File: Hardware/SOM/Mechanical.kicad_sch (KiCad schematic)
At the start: 1 part, among them J1 SODIMM-200_Split

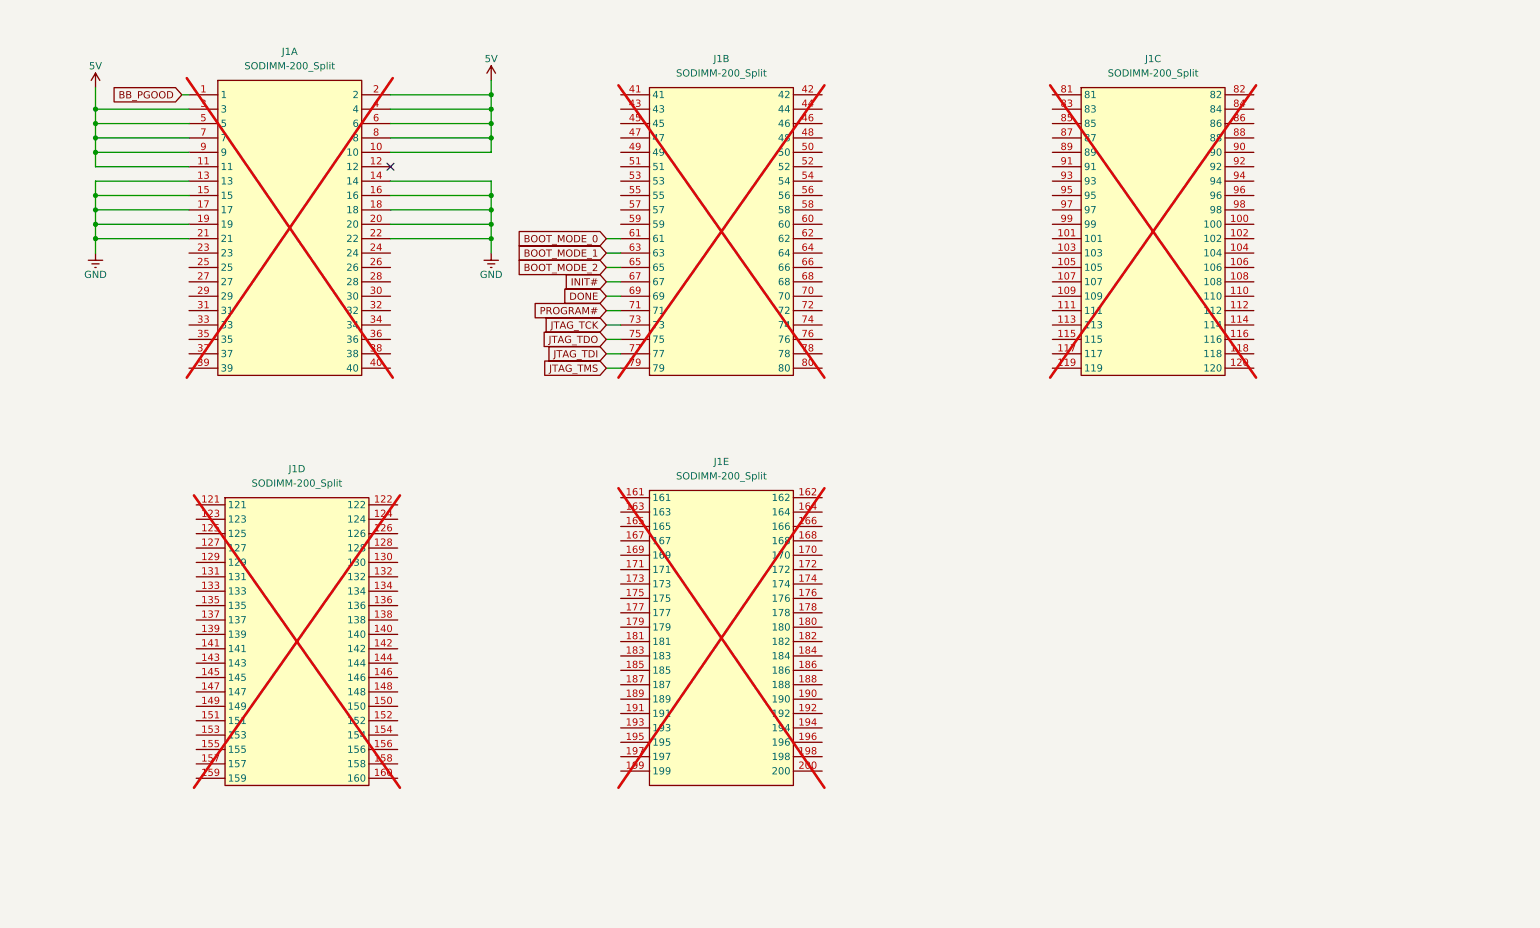
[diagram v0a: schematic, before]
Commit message: SOM: decoupling caps placement
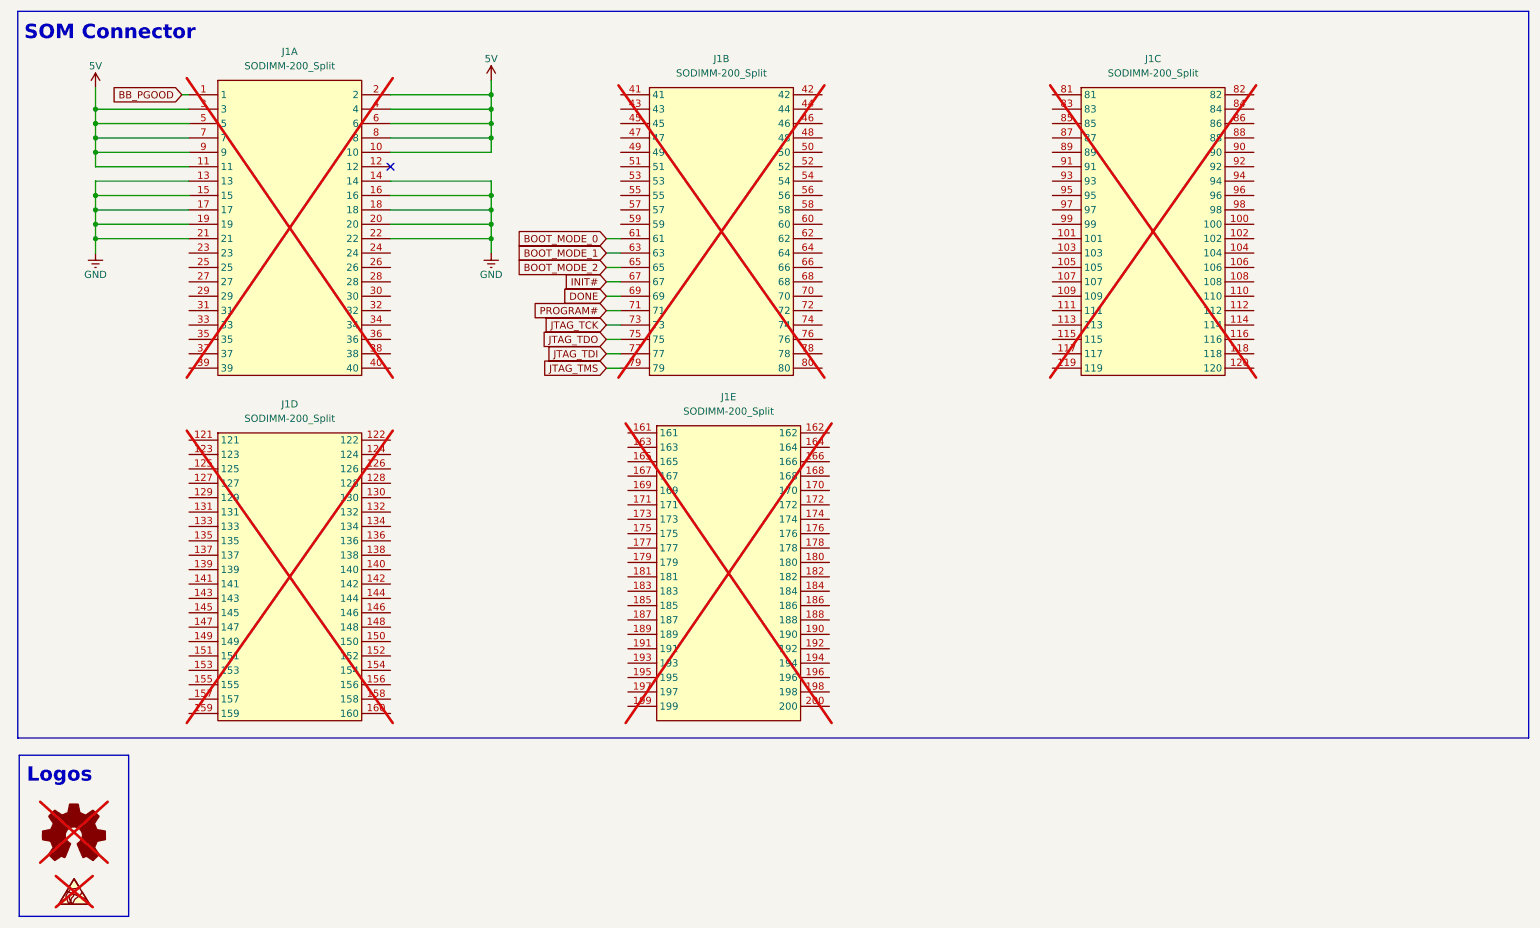
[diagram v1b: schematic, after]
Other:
- note added: "Logos"
- note added: "SOM Connector"
- moved on the sheet: J1D, J1E
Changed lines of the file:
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@@
 	(generator_version "9.0")
 	(paper "A4")
+	(rectangle
+		(start 15.494 15.748)
+		(end 282.194 144.018)
+		(stroke
+			(width 0)
+			(type default)
+		)
+		(fill
+			(type none)
+		)
+	)
+	(rectangle
+		(start 15.748 147.066)
+		(end 35.052 175.514)
+		(stroke
+			(width 0)
+			(type default)
+		)
+		(fill
+			(type none)
+		)
+	)
+	(text "Logos"
+		(exclude_from_sim no)
+		(at 22.86 150.622 0)
+		(effects
+			(font
+				(size 2.54 2.54)
+				(thickness 0.254)
+				(bold yes)
+			)
+		)
+	)
+	(text "SOM Connector"
+		(exclude_from_sim no)
+		(at 31.75 19.558 0)
+		(effects
+			(font
+				(size 2.54 2.54)
+				(thickness 0.254)
+				(bold yes)
+			)
+		)
+	)
 	(junction
 		(at 99.06 35.56)
@@
 	)
 	(symbol
+		(lib_id "Graphic:SYM_ESD_Small")
+		(at 25.4 171.45 0)
+		(unit 1)
+		(exclude_from_sim no)
+		(in_bom yes)
+		(on_board yes)
+		(dnp yes)
+		(fields_autoplaced yes)
+		(property "Reference" "#SYM2"
+			(at 25.4 167.894 0)
+			(effects
+				(font
+					(size 1.27 1.27)
+				)
+				(hide yes)
+			)
+		)
+		(property "Value" "SYM_ESD_Small"
+			(at 25.4 174.625 0)
+			(effects
+				(font
+					(size 1.27 1.27)
+				)
+				(hide yes)
+			)
+		)
+		(property "Footprint" "Symbol:ESD-Logo_6.6x6mm_SilkScreen"
+			(at 25.4 171.196 0)
+			(effects
+				(font
+					(size 1.27 1.27)
+				)
+				(hide yes)
+			)
+		)
+		(property "Datasheet" "~"
+			(at 25.4 171.196 0)
+			(effects
+				(font
+					(size 1.27 1.27)
+				)
+				(hide yes)
+			)
+		)
+		(property "Description" "ESD warning/\"Do not touch\" symbol, small"
+			(at 25.4 171.45 0)
+			(effects
+				(font
+					(size 1.27 1.27)
+				)
+				(hide yes)
+			)
+		)
+		(instances
+			(project ""
+				(path "/de32abb0-ff3b-4c67-a91a-eed08140b1b2/5afb2ac4-dadb-4f86-a03f-bc72f6fc34d4"
+					(reference "#SYM2")
+					(unit 1)
+				)
+			)
+		)
+	)
+	(symbol
 		(lib_id "power:+1V5")
 		(at 99.06 27.94 0)
@@
 	(symbol
 		(lib_id "Connector:SODIMM-200_Split")
-		(at 64.77 125.73 0)
+		(at 63.5 114.3 0)
 		(unit 4)
 		(exclude_from_sim no)
@@
 		(fields_autoplaced yes)
 		(property "Reference" "J1"
-			(at 64.77 96.52 0)
+			(at 63.5 85.09 0)
 			(effects
 				(font
@@
 		)
 		(property "Value" "SODIMM-200_Split"
-			(at 64.77 99.06 0)
+			(at 63.5 87.63 0)
 			(effects
 				(font
@@
 		)
 		(property "Footprint" "Connector_PCBEdge:SODIMM-200_1.8V_Card_edge"
-			(at 100.33 104.14 0)
+			(at 99.06 92.71 0)
 			(effects
 				(font
@@
 		)
 		(property "Datasheet" "~"
-			(at 100.33 104.14 0)
+			(at 99.06 92.71 0)
 			(effects
 				(font
@@
 		)
 		(property "Description" "SODIMM 200 Pin socket"
-			(at 64.77 125.73 0)
+			(at 63.5 114.3 0)
 			(effects
 				(font
@@
 		)
 		(property "Manufacturer" "TE Connectivity "
-			(at 64.77 125.73 0)
+			(at 63.5 114.3 0)
 			(effects
 				(font
@@
 		)
 		(property "MPN" "1473005-4 "
-			(at 64.77 125.73 0)
+			(at 63.5 114.3 0)
 			(effects
 				(font
@@
 					(reference "J1")
 					(unit 4)
+				)
+			)
+		)
+	)
+	(symbol
+		(lib_id "Graphic:Logo_Open_Hardware_Small")
+		(at 25.4 161.29 0)
+		(unit 1)
+		(exclude_from_sim no)
+		(in_bom yes)
+		(on_board yes)
+		(dnp yes)
+		(fields_autoplaced yes)
+		(property "Reference" "#SYM1"
+			(at 25.4 154.305 0)
+			(effects
+				(font
+					(size 1.27 1.27)
+				)
+				(hide yes)
+			)
+		)
+		(property "Value" "Logo_Open_Hardware_Small"
+			(at 25.4 167.005 0)
+			(effects
+				(font
+					(size 1.27 1.27)
+				)
+				(hide yes)
+			)
+		)
+		(property "Footprint" "Symbol:OSHW-Logo_5.7x6mm_Copper"
+			(at 25.4 161.29 0)
+			(effects
+				(font
+					(size 1.27 1.27)
+				)
+				(hide yes)
+			)
+		)
+		(property "Datasheet" "~"
+			(at 25.4 161.29 0)
+			(effects
+				(font
+					(size 1.27 1.27)
+				)
+				(hide yes)
+			)
+		)
+		(property "Description" "Open Hardware logo, small"
+			(at 25.4 161.29 0)
+			(effects
+				(font
+					(size 1.27 1.27)
+				)
+				(hide yes)
+			)
+		)
+		(instances
+			(project ""
+				(path "/de32abb0-ff3b-4c67-a91a-eed08140b1b2/5afb2ac4-dadb-4f86-a03f-bc72f6fc34d4"
+					(reference "#SYM1")
+					(unit 1)
 				)
 			)
@@
 	(symbol
 		(lib_id "Connector:SODIMM-200_Split")
-		(at 139.7 124.46 0)
+		(at 140.97 113.03 0)
 		(unit 5)
 		(exclude_from_sim no)
@@
 		(fields_autoplaced yes)
 		(property "Reference" "J1"
-			(at 139.7 95.25 0)
+			(at 140.97 83.82 0)
 			(effects
 				(font
@@
 		)
 		(property "Value" "SODIMM-200_Split"
-			(at 139.7 97.79 0)
+			(at 140.97 86.36 0)
 			(effects
 				(font
@@
 		)
 		(property "Footprint" "Connector_PCBEdge:SODIMM-200_1.8V_Card_edge"
-			(at 175.26 102.87 0)
+			(at 176.53 91.44 0)
 			(effects
 				(font
@@
 		)
 		(property "Datasheet" "~"
-			(at 175.26 102.87 0)
+			(at 176.53 91.44 0)
 			(effects
 				(font
@@
 		)
 		(property "Description" "SODIMM 200 Pin socket"
-			(at 139.7 124.46 0)
+			(at 140.97 113.03 0)
 			(effects
 				(font
@@
 		)
 		(property "Manufacturer" "TE Connectivity "
-			(at 139.7 124.46 0)
+			(at 140.97 113.03 0)
 			(effects
 				(font
@@
 		)
 		(property "MPN" "1473005-4 "
-			(at 139.7 124.46 0)
-			(effects
-				(font
+			(at 140.97 113.03 0)
+			(effects
+				(font
